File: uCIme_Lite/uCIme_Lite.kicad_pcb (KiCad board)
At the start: 4 copper layers, 65 x 56 mm, 72 parts, among them J1 USB_MODE, J10 JACK_MODE, J11 SERIAL_MODE, J12 SERIAL_VOLTAGE_SELECT, J2 JACK_POWER_IN, J3 USB_POWER_IN, J4 USB_PC, J6 5V_ENABLE, J7 SERIAL_AND_GPIO, J8 JACK_POWER_OUT, J9 USB_POWER_OUT, Q1 BSS138, Q2 BUK7M27-80EX, Q3 BUK7M27-80EX, Q4 BSS138, Q5 BSS138, Q6 BSS138, Q7 BSS138, Q8 BSS138, U1 LM74502, U2 LM74502, U3 AP2204K-ADJ, U4 AP2204K-ADJ, U5 FT230XS, U6 TXB0104D

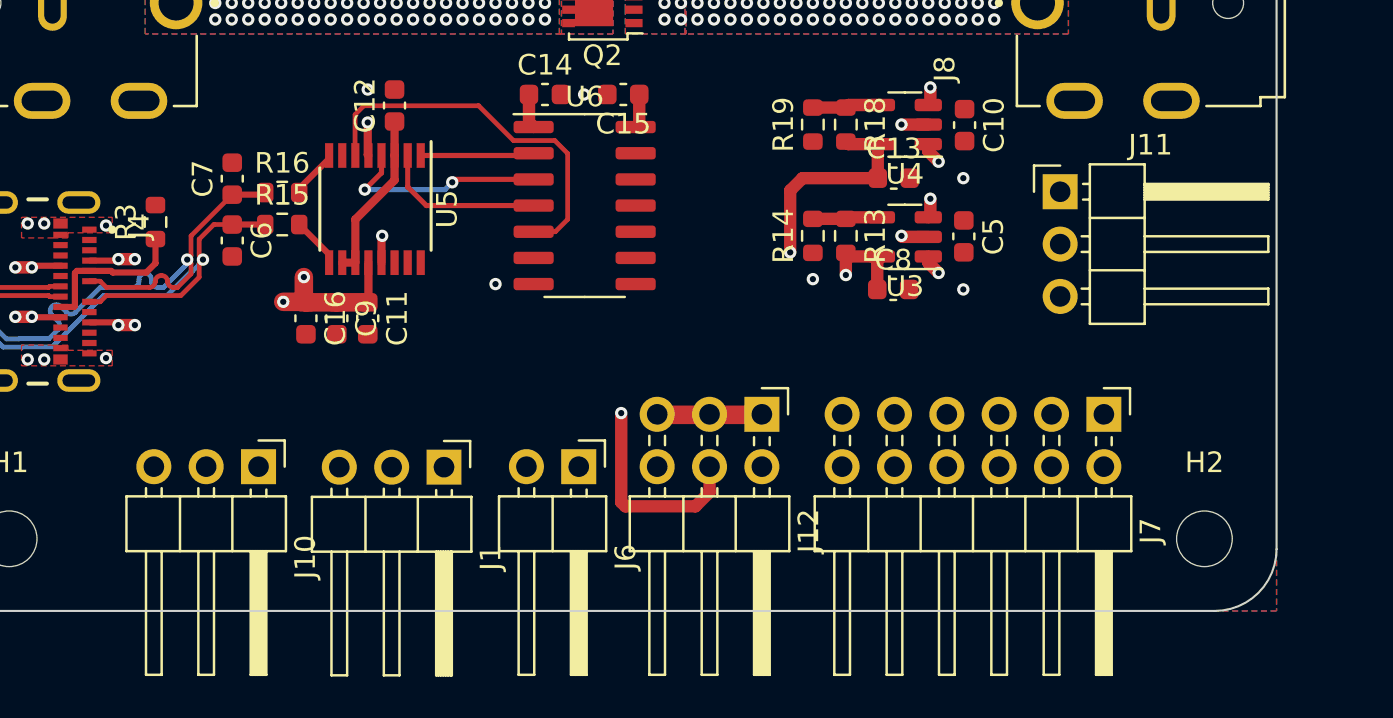
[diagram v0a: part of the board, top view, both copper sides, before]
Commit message: lite: Updated jack and USB power double-row pin header connector in PCB.
Signed-off-by: Adrien Ricciardi <aricciardi@baylibre.com>
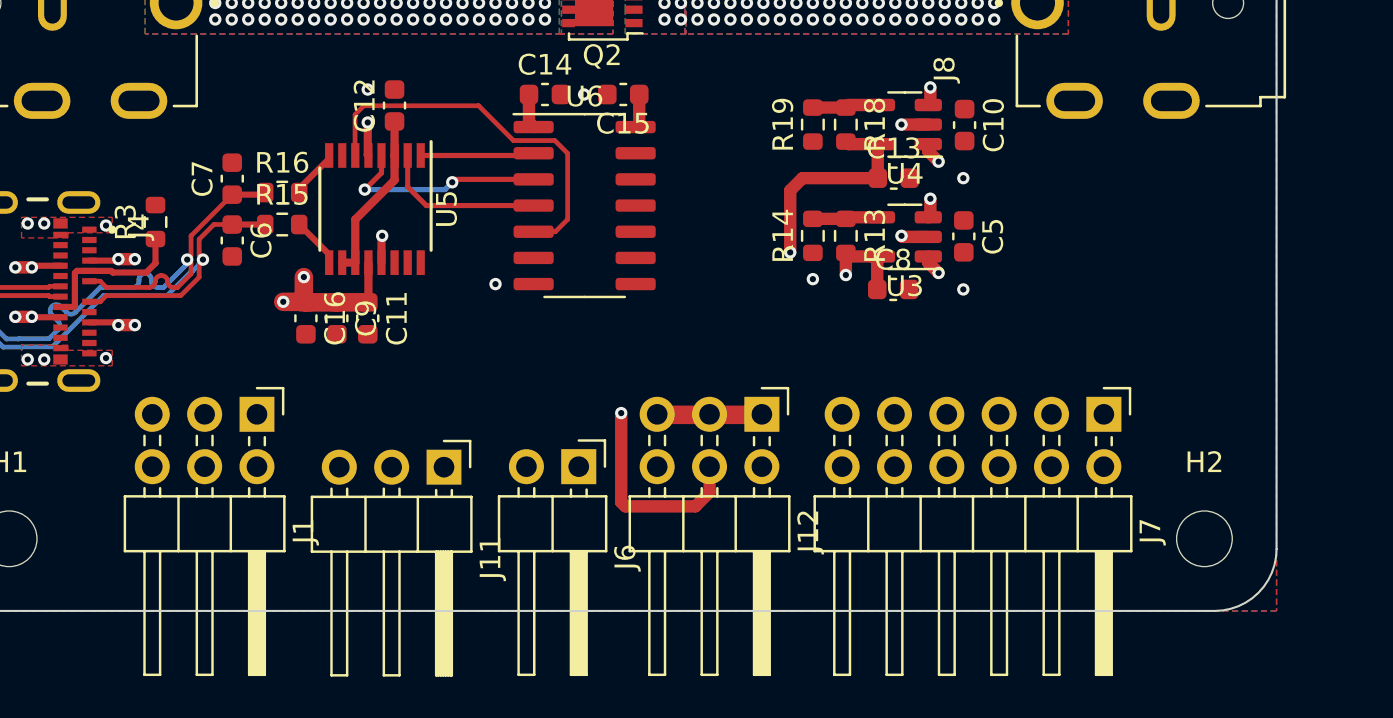
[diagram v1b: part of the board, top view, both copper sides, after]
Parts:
- removed J10: JACK_MODE, Connector_PinHeader_2.54mm:PinHeader_1x03_P2.54mm_Horizontal
- J1: value USB_MODE -> POWER_MODES; footprint Connector_PinHeader_2.54mm:PinHeader_1x03_P2.54mm_Horizontal -> Connector_PinHeader_2.54mm:PinHeader_2x03_P2.54mm_Horizontal
- moved J11 32.8 mm to (89.6, 106.0), turned to -90 degrees
- moved J1 9.43 mm to (80.5, 103.5)
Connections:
- J1 pad 2: Net-(J1-Pin_2) -> +5V
- J1 pad 3: /Controller/GPIO_0 -> Net-(J1-Pin_3)
- Q1 pad 1: Net-(J10-Pin_2) -> Net-(J1-Pin_4)
- Q4 pad 1: Net-(J1-Pin_2) -> Net-(J1-Pin_3)
- R2 pad 1: Net-(J1-Pin_2) -> Net-(J1-Pin_3)
- R9 pad 1: Net-(J10-Pin_2) -> Net-(J1-Pin_4)
- U1 pad 1: Net-(J10-Pin_2) -> Net-(J1-Pin_4)
- U2 pad 1: Net-(J1-Pin_2) -> Net-(J1-Pin_3)

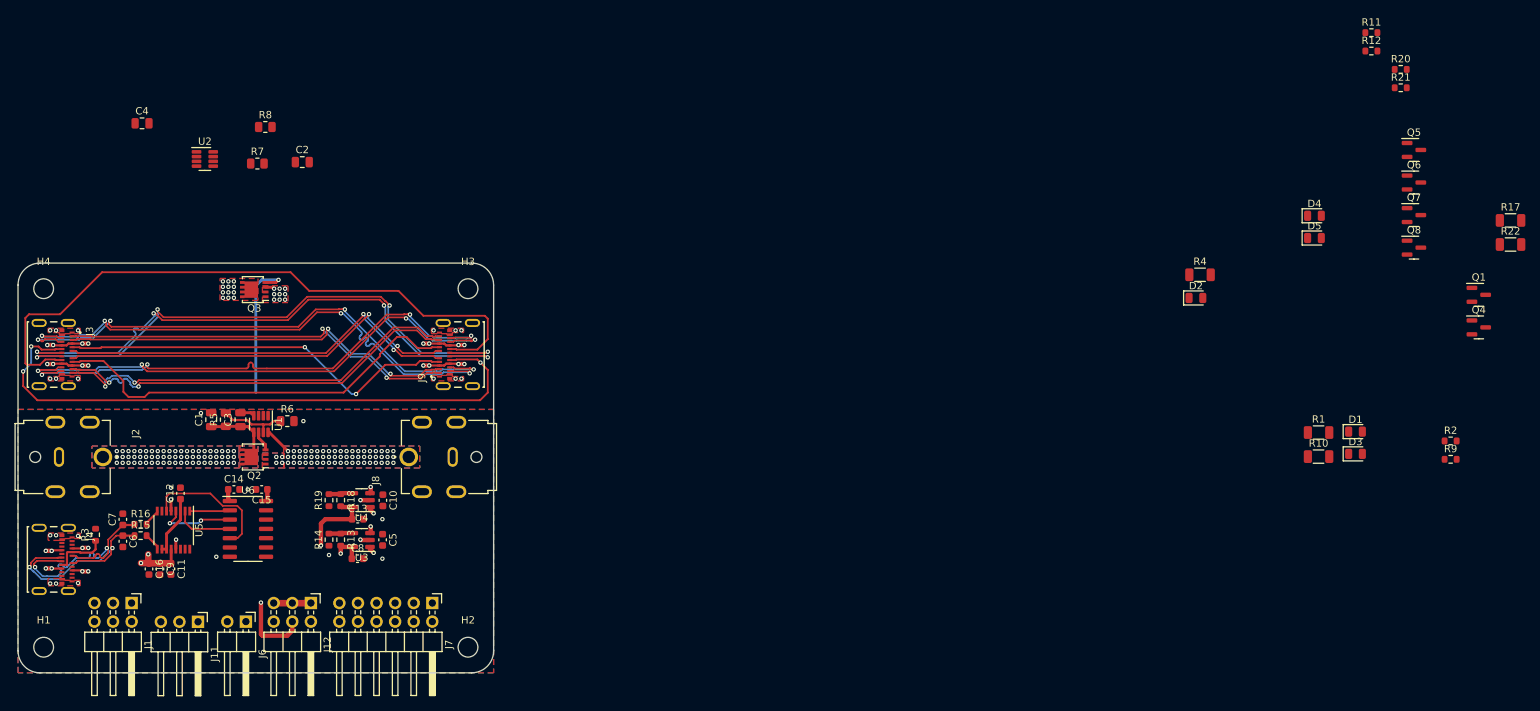
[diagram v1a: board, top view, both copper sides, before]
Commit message: lite: Routed USB power channel gate driver.
Signed-off-by: Adrien Ricciardi <aricciardi@baylibre.com>
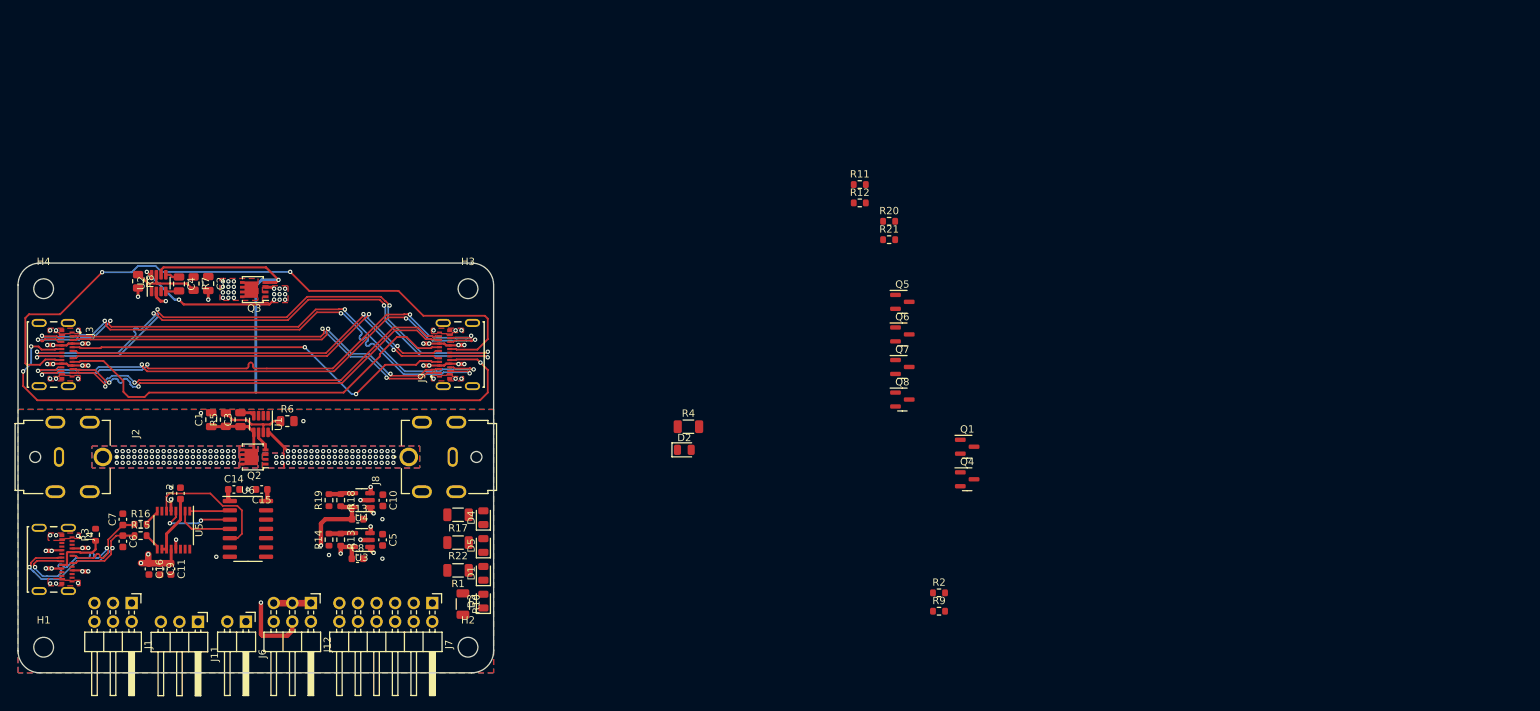
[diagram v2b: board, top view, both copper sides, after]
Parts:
- moved R22 149.5 mm to (125.1, 95.2), turned to 180 degrees
- moved R17 149.4 mm to (125.1, 91.4), turned to 180 degrees
- moved D5 121.1 mm to (128.6, 95.6), turned to 90 degrees
- moved D? 120.9 mm to (128.6, 103.2), turned to 90 degrees
- moved D4 120.8 mm to (128.6, 91.8), turned to 90 degrees
- moved D? 120.8 mm to (128.6, 99.4), turned to 90 degrees
- moved R1 119.1 mm to (125.1, 99.0), turned to 180 degrees
- moved R10 118.7 mm to (125.8, 103.6), turned to -90 degrees
- moved D2 72.9 mm to (156.1, 82.5)
- moved R11 72.9 mm to (180.0, 46.3)
- moved R12 72.9 mm to (180.0, 48.8)
- moved R9 72.9 mm to (190.9, 104.6)
- moved R2 72.9 mm to (190.9, 102.1)
- moved Q1 72.9 mm to (194.7, 82.1)
- moved Q4 72.9 mm to (194.7, 86.5)
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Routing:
- net /Power Management/OUTPUT_USB_V+: track 12.7 -> 33.0 mm, vias 17 -> 19
- net Net-(Q3-G): track 20.0 -> 37.5 mm
- net Net-(U2-OV): track 0.00 -> 10.4 mm
- net GND: track 5.55 -> 10.3 mm, vias 30 -> 33
- net /Power Management/INPUT_USB_V+: track 11.4 -> 13.4 mm
- net Net-(U2-VCAP): track 0.00 -> 1.83 mm
- net /CC2: track 88.6 -> 89.4 mm, vias 0 -> 2

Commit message: lite: Placed leds and related transistors onto the PCB.
Signed-off-by: Adrien Ricciardi <aricciardi@baylibre.com>
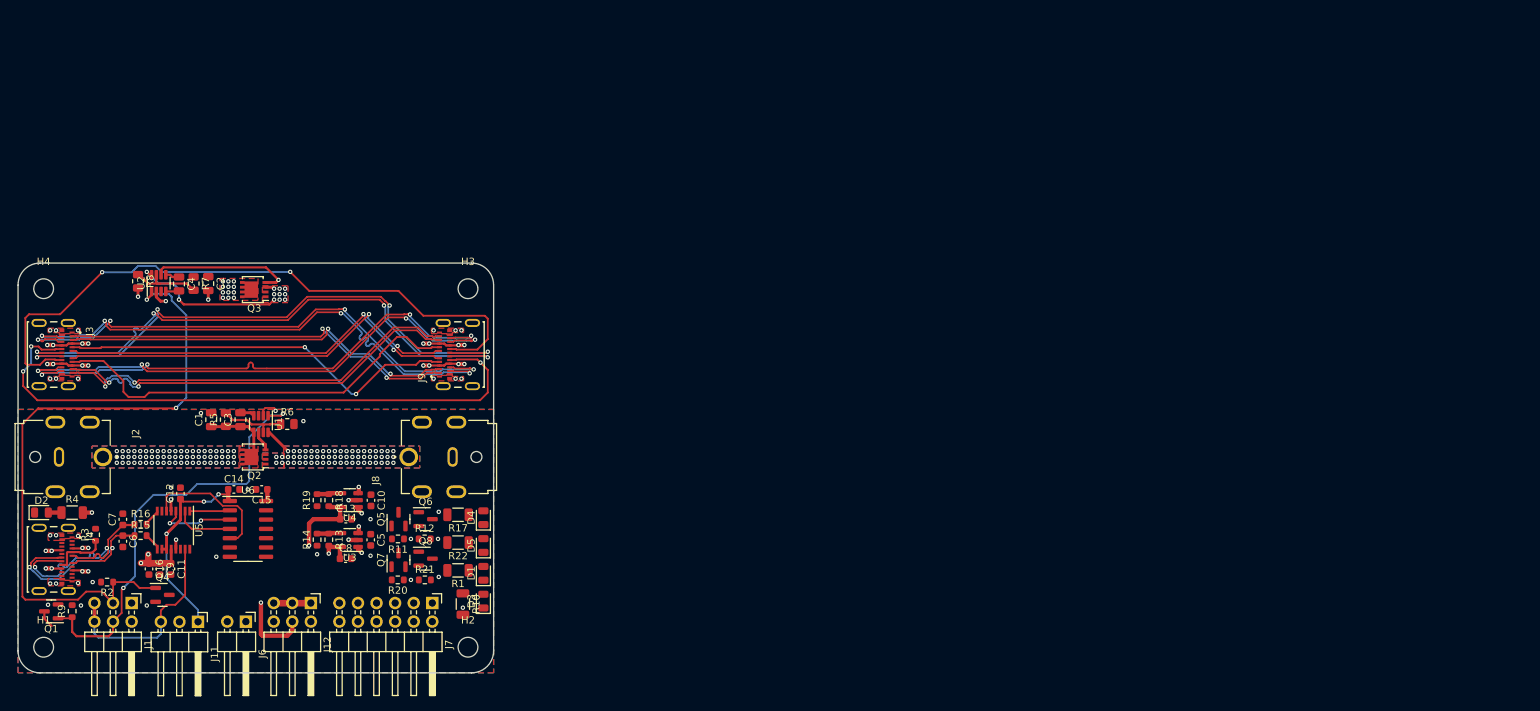
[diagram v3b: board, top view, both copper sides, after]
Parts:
- moved Q1 127.2 mm to (69.5, 104.6), turned to 180 degrees
- moved R9 118.5 mm to (72.4, 104.6), turned to 90 degrees
- moved R2 113.7 mm to (77.2, 100.6), turned to 180 degrees
- moved Q4 111.1 mm to (84.7, 102.3)
- moved D2 88.3 mm to (68.2, 91.1)
- moved R4 85.0 mm to (72.4, 91.1)
- moved R20 83.1 mm to (116.9, 100.3), turned to 180 degrees
- moved R11 79.6 mm to (116.9, 94.7), turned to 180 degrees
- moved R21 78.7 mm to (120.6, 100.3)
- moved R12 75.1 mm to (120.6, 94.7)
- moved Q5 75.0 mm to (117.0, 92.0), turned to 90 degrees
- moved Q7 73.7 mm to (117.0, 97.6), turned to 90 degrees
- moved Q6 69.9 mm to (120.7, 92.0)
- moved Q8 68.7 mm to (120.7, 97.4)
- moved C10 1.62 mm to (113.2, 89.4)
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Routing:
- net Net-(J1-Pin_3): track 0.00 -> 90.1 mm, vias 0 -> 2
- net Net-(J1-Pin_4): track 0.00 -> 59.0 mm, vias 0 -> 2
- net /Controller/GPIO_0: track 0.00 -> 27.4 mm
- net +3.3VA: track 9.95 -> 30.8 mm, vias 0 -> 3
- net Net-(Q3-G): track 37.5 -> 19.5 mm
- net +3.3V: track 35.2 -> 21.1 mm
- net +1V8: track 12.7 -> 7.56 mm
- net GND: track 10.3 -> 13.1 mm, vias 33 -> 40
- net Net-(D1-K): track 0.00 -> 2.41 mm
- net Net-(D2-A): track 0.00 -> 1.80 mm
- net +5V: track 20.2 -> 21.4 mm, vias 14 -> 19
- net /Power Management/OUTPUT_USB_V+: track 33.0 -> 33.9 mm
- net Net-(U1-OV): track 9.83 -> 9.27 mm

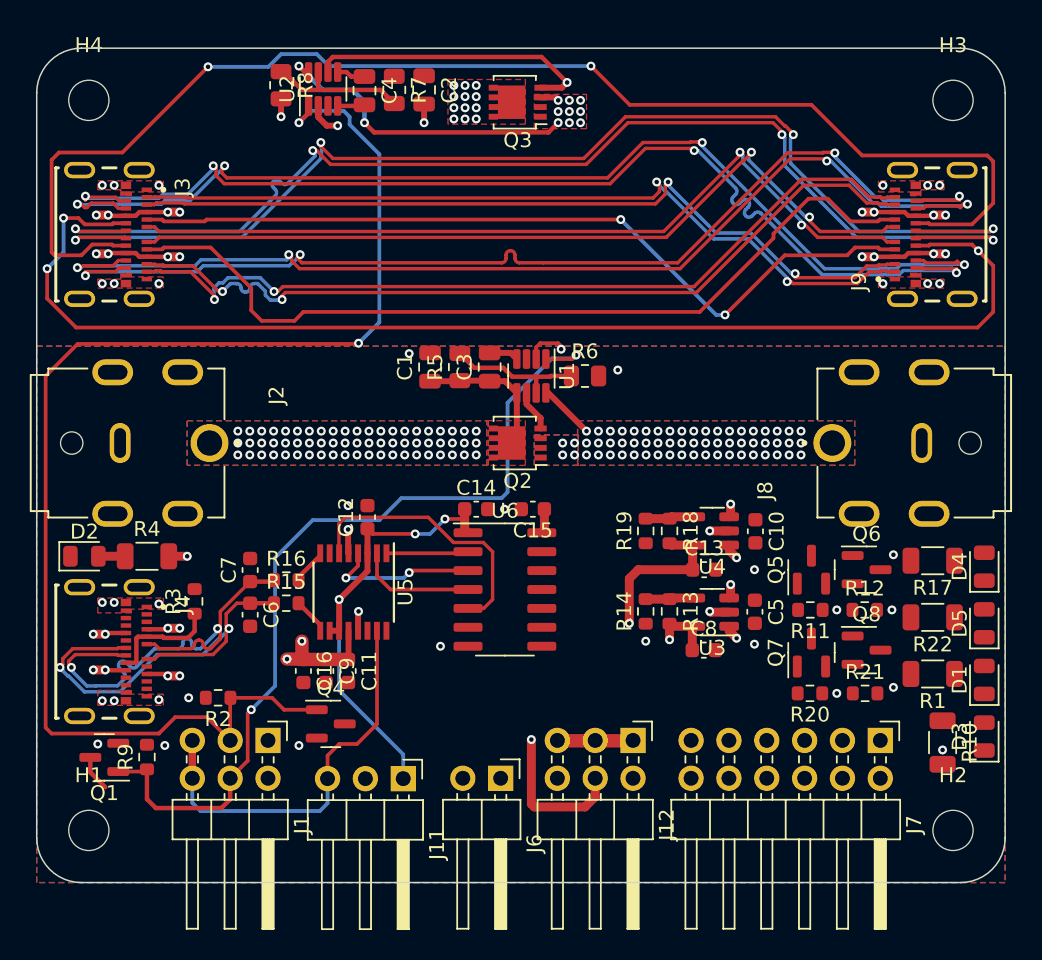
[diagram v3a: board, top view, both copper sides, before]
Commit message: lite: Routed the leds and fixed some of the PCB warnings.
Signed-off-by: Adrien Ricciardi <aricciardi@baylibre.com>
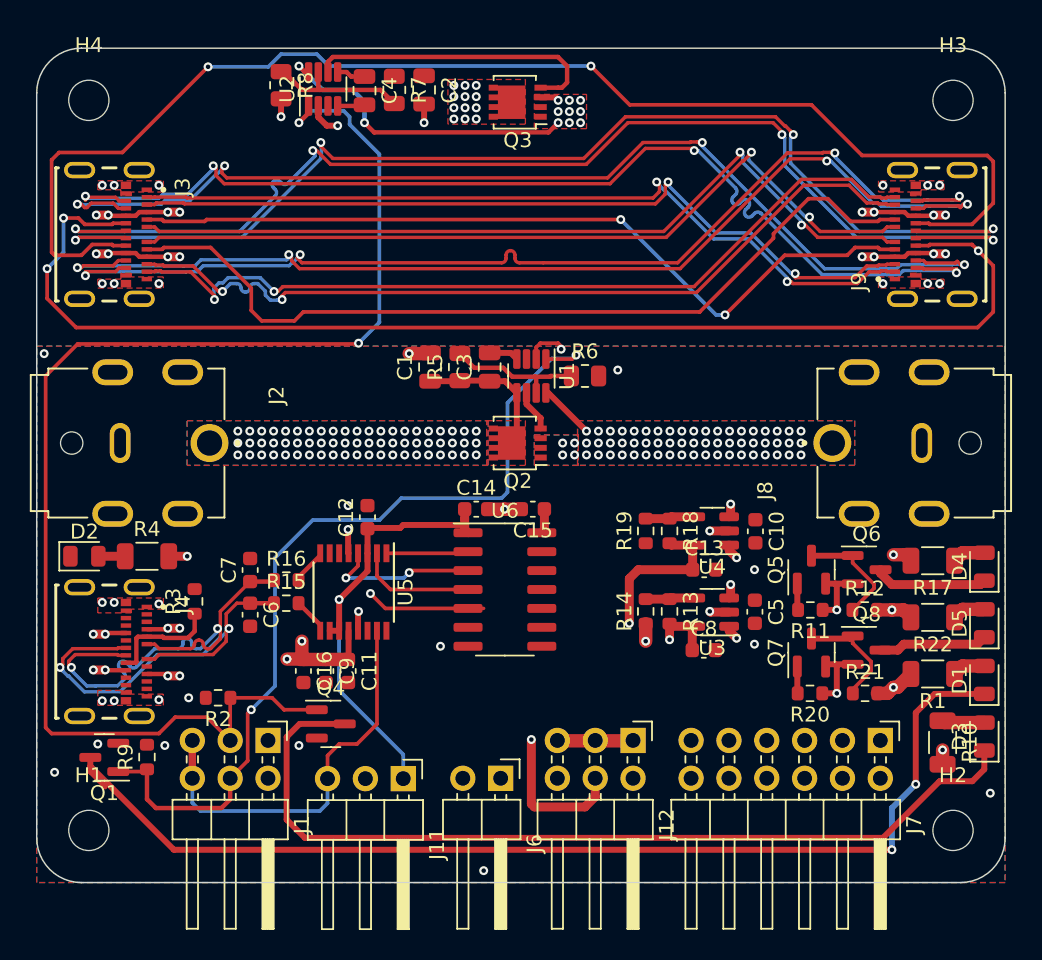
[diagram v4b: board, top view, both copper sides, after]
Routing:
- net Net-(D1-K): track 2.41 -> 74.1 mm, vias 0 -> 2
- net Net-(D3-K): track 0.00 -> 60.3 mm
- net GND: track 13.1 -> 27.4 mm, vias 40 -> 44
- net Net-(U5-~{CTS}): track 18.5 -> 8.01 mm, vias 0 -> 1
- net Net-(Q7-D): track 0.00 -> 7.70 mm
- net Net-(D4-K): track 0.00 -> 7.62 mm
- net Net-(Q5-D): track 0.00 -> 7.61 mm
- net +5V: track 21.4 -> 29.0 mm
- net Net-(D5-K): track 0.00 -> 7.32 mm
- net Net-(D3-A): track 0.00 -> 2.85 mm
- net Net-(D5-A): track 0.00 -> 2.22 mm
- net Net-(D4-A): track 0.00 -> 2.22 mm
- net Net-(D1-A): track 0.00 -> 2.22 mm
- net /Controller/UART_TX: track 5.52 -> 7.33 mm
- net /Controller/UART_RX: track 10.4 -> 12.2 mm
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
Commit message: lite: Finished routing all remaining signals.
Signed-off-by: Adrien Ricciardi <aricciardi@baylibre.com>
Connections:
- Q5 pad 1: /Controller/UART_RX -> /Controller/UART_TX
- Q7 pad 1: /Controller/UART_TX -> /Controller/UART_RX
- R11 pad 2: /Controller/UART_RX -> /Controller/UART_TX
- R20 pad 2: /Controller/UART_TX -> /Controller/UART_RX
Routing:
- net /Controller/GPIO_2: track 0.00 -> 46.8 mm, vias 0 -> 2
- net /Controller/GPIO_0: track 27.4 -> 65.1 mm, vias 0 -> 1
- net /Controller/GPIO_1: track 0.00 -> 32.7 mm, vias 0 -> 1
- net /Controller/GPIO_3: track 0.00 -> 31.2 mm
- net /Controller/UART_RX: track 12.2 -> 38.7 mm, vias 2 -> 4
- net /Controller//SERIAL_CTS: track 0.00 -> 26.2 mm
- net Net-(J6-Pin_1): track 0.00 -> 24.7 mm
- net /Controller/SERIAL_TX: track 0.00 -> 23.3 mm
- net /Controller/UART_TX: track 7.33 -> 30.3 mm, vias 0 -> 2
- net Net-(J12-Pin_1): track 6.73 -> 26.8 mm
- net /Controller/SERIAL_RX: track 0.00 -> 19.7 mm
- net Net-(J11-Pin_2): track 0.00 -> 18.3 mm, vias 0 -> 2
- net /Controller//SERIAL_RTS: track 0.00 -> 16.9 mm
- net +3.3V: track 21.1 -> 31.6 mm
- net +1V8: track 7.56 -> 15.8 mm, vias 1 -> 2
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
